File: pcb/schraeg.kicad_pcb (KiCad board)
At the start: 2 copper layers, 83.8 x 128.5 mm, 136 parts, among them J1 PJ398SM, J2 PJ398SM, J3 PJ398SM, J4 PJ398SM, J5 PJ398SM, J6 PJ398SM, J7 PJ398SM, J8 POWER, SW1 CS12ANW03, SW2 CS12ANW03, SW3 CS12ANW03, U1 TL074, U2 TL074, U3 V2164, U4 TL074, U5 TL074, U6 LM321

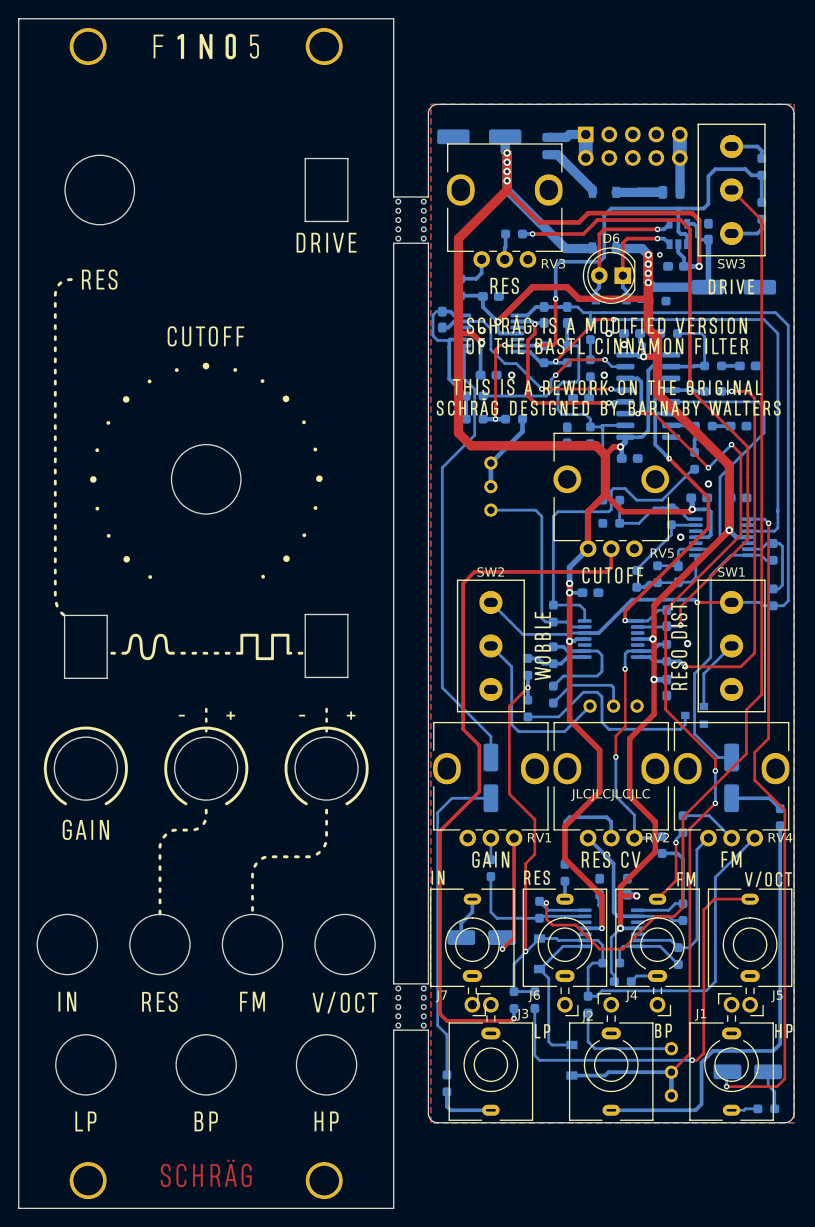
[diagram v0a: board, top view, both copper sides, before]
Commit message: Removed copper on the panel mounting holes
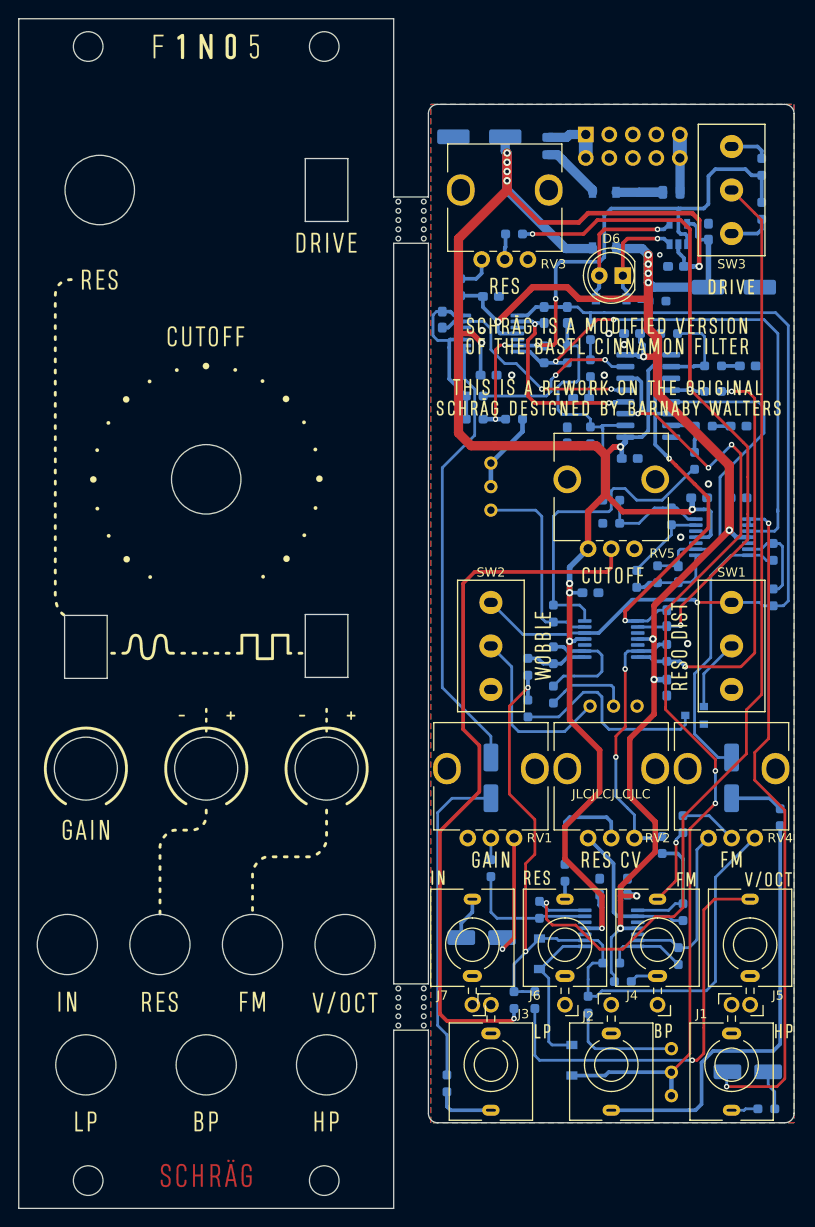
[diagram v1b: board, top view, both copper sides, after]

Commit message: Version 0.3.1
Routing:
- net GND: vias 9 -> 8

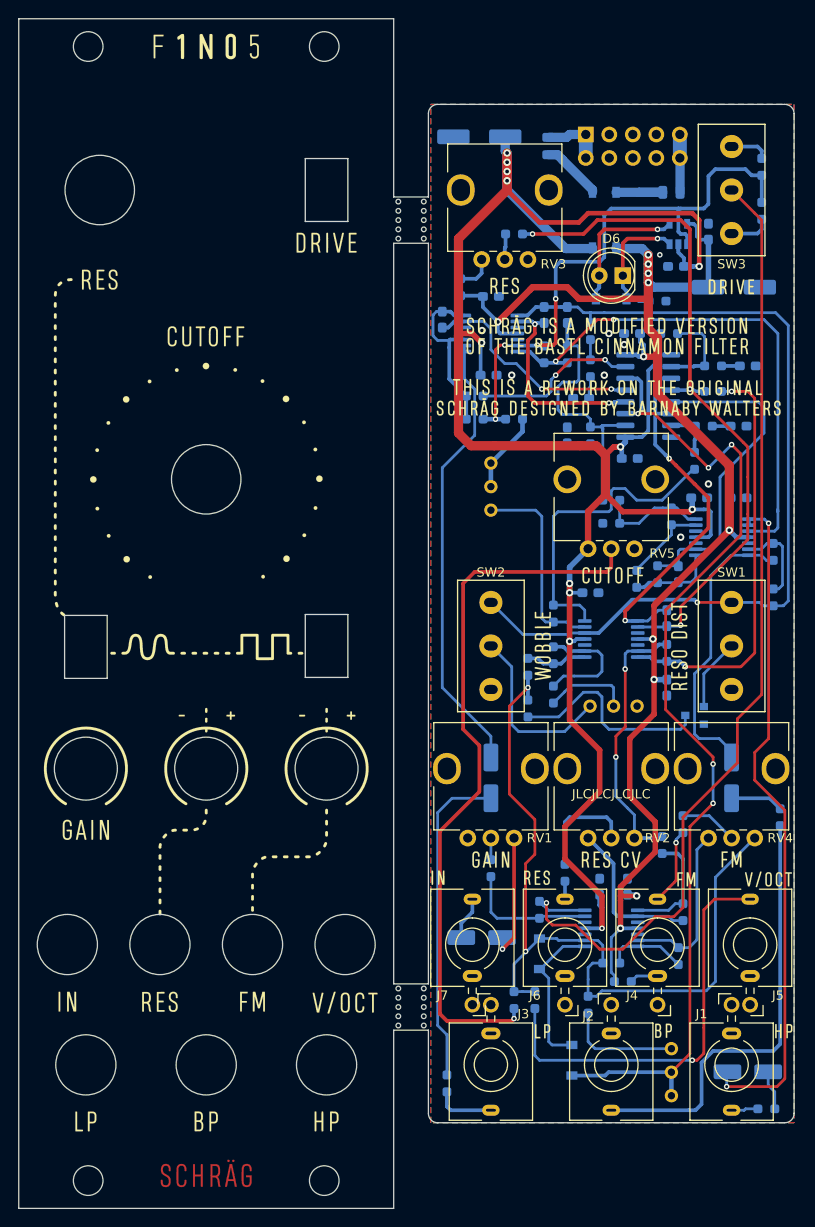
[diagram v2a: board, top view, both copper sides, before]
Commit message: Only one row of mouse bites
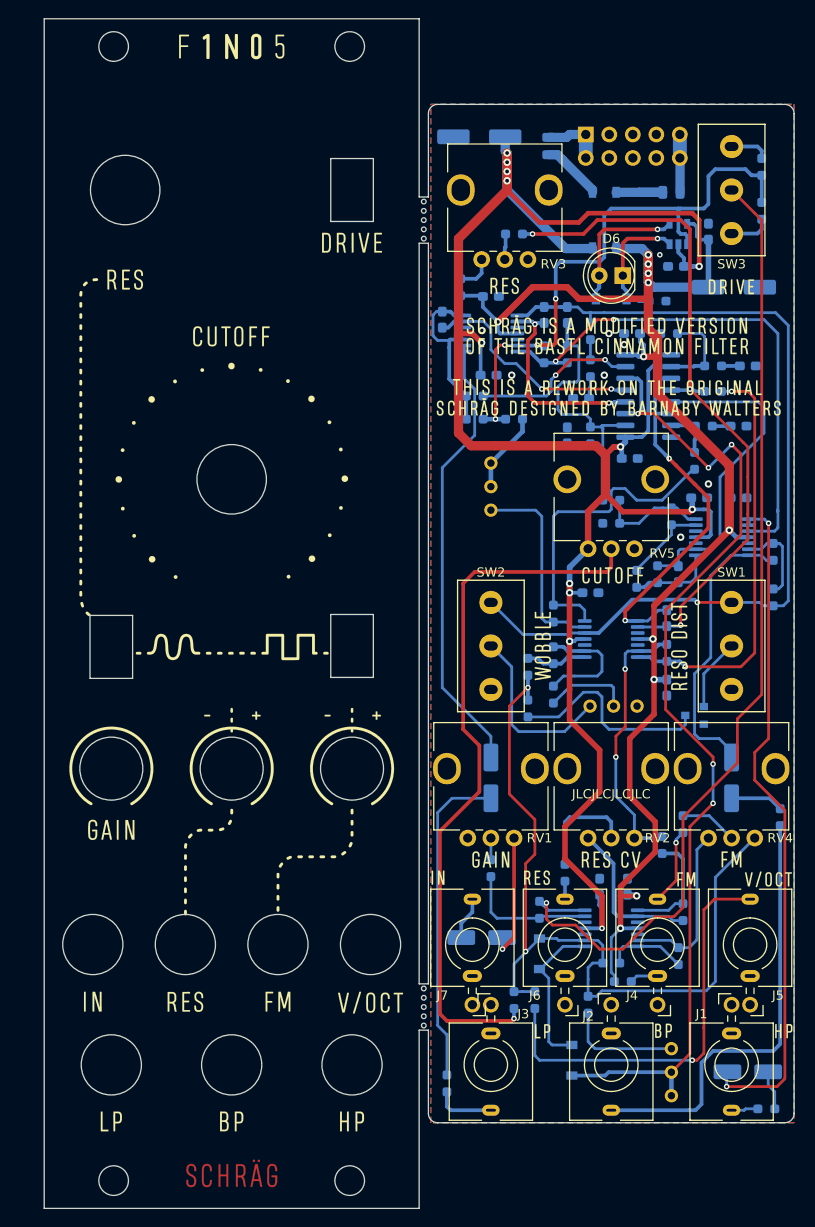
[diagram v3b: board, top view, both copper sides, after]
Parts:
- removed the REF** at (96.8, 145.5)
- removed the REF** at (96.8, 64.5)
- removed the REF** at (96.8, 63.5)
- removed the REF** at (96.8, 62.5)
- removed the REF** at (96.8, 61.5)
- removed the REF** at (88.8, 166.2)
- removed the REF** at (63.2, 166.2)
- removed the REF** at (88.8, 43.8)
- removed the REF** at (96.8, 60.5)
- removed the REF** at (96.8, 149.5)
- removed the REF** at (96.8, 148.5)
- removed the REF** at (96.8, 147.5)
- removed the REF** at (96.8, 146.5)
- added REF**: MountingHole_3.2mm_M3, MountingHole:MountingHole_3.2mm_M3, F.Cu at (91.5, 166.2)
- added REF**: MountingHole_3.2mm_M3, MountingHole:MountingHole_3.2mm_M3, F.Cu at (66.0, 166.2)
- added REF**: MountingHole_3.2mm_M3, MountingHole:MountingHole_3.2mm_M3, F.Cu at (91.5, 43.8)
- moved G*** 2.75 mm to (78.8, 105.0) (x4)
- moved REF** 2.75 mm to (66.0, 43.8)
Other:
- board size 83.8 x 128.5 mm -> 81 x 128.5 mm

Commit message: #13 -  Halved FM input range
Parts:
- R2, R48, R5: value 47K -> 100K
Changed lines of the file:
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@@
-(kicad_pcb (version 20171130) (host pcbnew 5.1.10-88a1d61d58~90~ubuntu21.04.1)
+(kicad_pcb (version 20171130) (host pcbnew 5.1.12-84ad8e8a86~92~ubuntu21.04.1)
   (general
     (thickness 1.6)
@@
     (tags SOT-23-5)
     (attr smd)
-    (fp_text reference U6 (at 2.5 0 180) (layer B.SilkS)
+    (fp_text reference U6 (at 0 -3 270) (layer B.SilkS)
       (effects (font (size 1 1) (thickness 0.15)) (justify mirror))
     )
@@
       (effects (font (size 1 1) (thickness 0.15)) (justify mirror))
     )
-    (fp_text value 47K (at 0 -1.43 90) (layer B.Fab)
+    (fp_text value 100K (at 0 -1.43 90) (layer B.Fab)
       (effects (font (size 1 1) (thickness 0.15)) (justify mirror))
     )
@@
       (effects (font (size 1 1) (thickness 0.15)) (justify mirror))
     )
-    (fp_text value 47K (at 0 -1.43) (layer B.Fab)
+    (fp_text value 100K (at 0 -1.43) (layer B.Fab)
       (effects (font (size 1 1) (thickness 0.15)) (justify mirror))
     )
@@
       (effects (font (size 1 1) (thickness 0.15)) (justify mirror))
     )
-    (fp_text value 47K (at 0 -1.43 90) (layer B.Fab)
+    (fp_text value 100K (at 0 -1.43 90) (layer B.Fab)
       (effects (font (size 1 1) (thickness 0.15)) (justify mirror))
     )
